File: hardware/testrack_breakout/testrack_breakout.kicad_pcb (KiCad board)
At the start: 4 copper layers, 40 x 78 mm, 15 parts, among them J1 USB_C_Receptacle_USB2.0_16P, J2 Conn_02x05_Odd_Even, J3 Conn_02x10_Odd_Even, J4 Conn_01x04, J5 Conn_02x09_Odd_Even

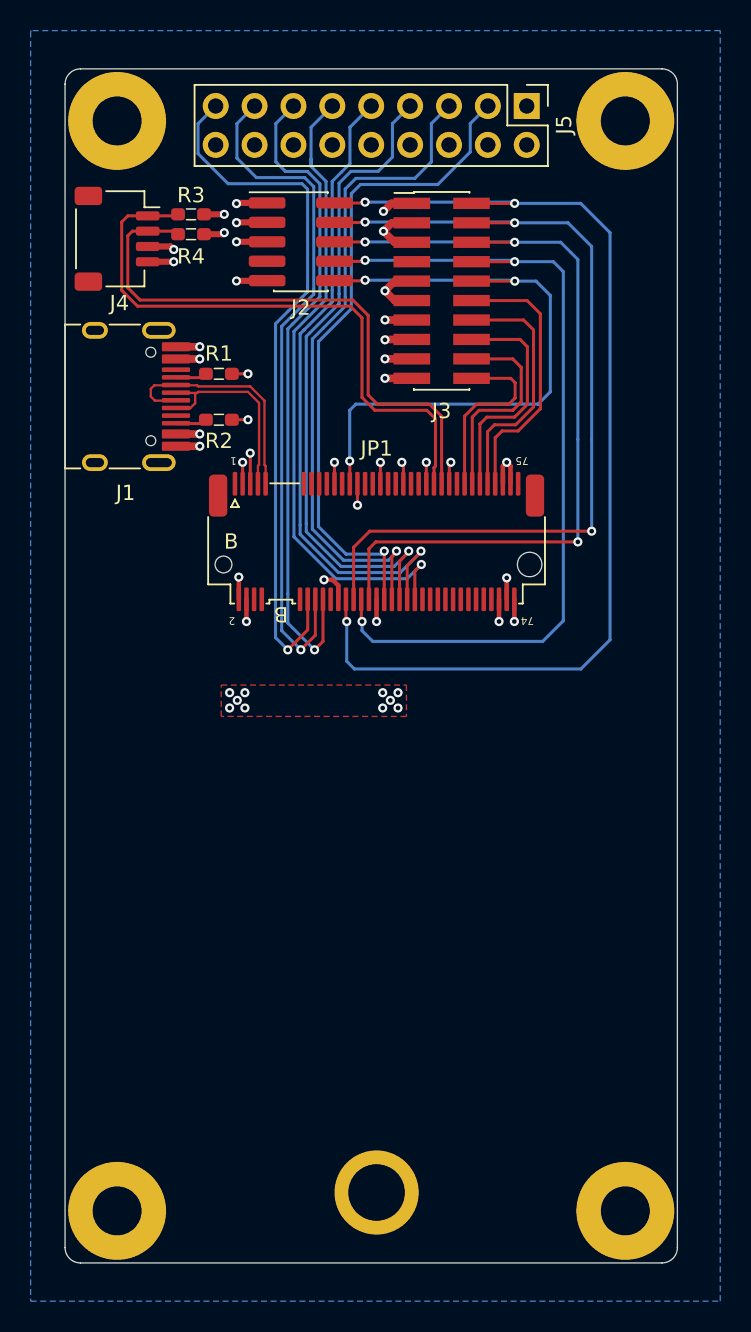
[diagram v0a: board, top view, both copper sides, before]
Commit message: Added board identification to the silkscreen
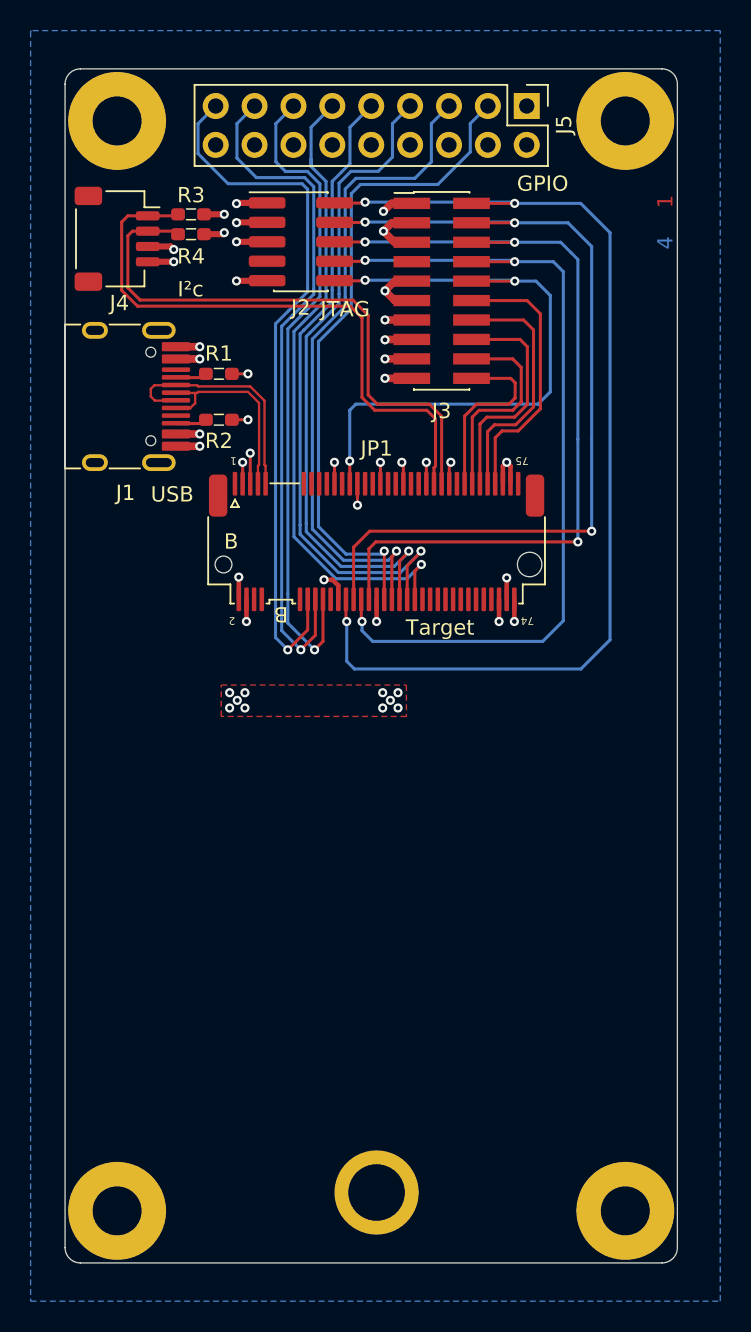
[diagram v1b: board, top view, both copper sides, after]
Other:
- board text added: "1"
- board text added: "1BitSquared"
- board text added: "2"
- board text added: "3"
- board text added: "4"
- board text added: "CERN OHL v2 Strict"
- board text added: "GPIO"
- board text added: "I²c"
- board text added: "JTAG"
- board text added: "License"
- board text added: "RWK"
- board text added: "Target"
- board text added: "USB"
- board text added: "testrack_breakout"
- board text added: "v0.1a"
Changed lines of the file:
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@@
 		(embedded_fonts no)
 	)
+	(gr_rect
+		(start 88.6 58.5)
+		(end 90.1 62.3)
+		(stroke
+			(width 0)
+			(type solid)
+		)
+		(fill yes)
+		(layer "F.Mask")
+	)
+	(gr_rect
+		(start 88.6 58.5)
+		(end 90.1 62.3)
+		(stroke
+			(width 0)
+			(type solid)
+		)
+		(fill yes)
+		(layer "B.Mask")
+	)
+	(gr_line
+		(start 70.2 98.5)
+		(end 70.2 110.6)
+		(stroke
+			(width 0.1)
+			(type default)
+		)
+		(layer "B.SilkS")
+	)
+	(gr_rect
+		(start 67.6 107)
+		(end 69.6 109.1)
+		(stroke
+			(width 0)
+			(type solid)
+		)
+		(fill yes)
+		(layer "B.SilkS")
+	)
 	(gr_arc
 		(start 90.2 127.5)
@@
 		(layer "Edge.Cuts")
 	)
+	(gr_text "1"
+		(at 90 59.6 90)
+		(layer "F.Cu")
+		(effects
+			(font
+				(size 1 1)
+				(thickness 0.15)
+			)
+			(justify left bottom)
+		)
+	)
+	(gr_text "4"
+		(at 90 62.3 90)
+		(layer "B.Cu")
+		(effects
+			(font
+				(size 1 1)
+				(thickness 0.15)
+			)
+			(justify left bottom)
+		)
+	)
+	(gr_text "2"
+		(at 90 60.5 90)
+		(layer "In1.Cu")
+		(effects
+			(font
+				(size 1 1)
+				(thickness 0.15)
+			)
+			(justify left bottom)
+		)
+	)
+	(gr_text "I²c"
+		(at 58.4 64.9 0)
+		(layer "F.SilkS")
+		(effects
+			(font
+				(size 1 1)
+				(thickness 0.1)
+			)
+		)
+	)
+	(gr_text "GPIO"
+		(at 81.4 58 0)
+		(layer "F.SilkS")
+		(effects
+			(font
+				(size 1 1)
+				(thickness 0.1)
+			)
+		)
+	)
+	(gr_text "JTAG"
+		(at 68.5 66.2 0)
+		(layer "F.SilkS")
+		(effects
+			(font
+				(size 1 1)
+				(thickness 0.1)
+			)
+		)
+	)
+	(gr_text "Target"
+		(at 74.7 87 0)
+		(layer "F.SilkS")
+		(effects
+			(font
+				(size 1 1)
+				(thickness 0.1)
+			)
+		)
+	)
+	(gr_text "USB"
+		(at 57.2 78.3 0)
+		(layer "F.SilkS")
+		(effects
+			(font
+				(size 1 1)
+				(thickness 0.1)
+			)
+		)
+	)
+	(gr_text "3"
+		(at 90 61.4 90)
+		(layer "In2.Cu")
+		(effects
+			(font
+				(size 1 1)
+				(thickness 0.15)
+			)
+			(justify left bottom)
+		)
+	)
+	(gr_text "1BitSquared"
+		(at 70 99.8 -0)
+		(layer "B.SilkS")
+		(effects
+			(font
+				(size 1 1)
+				(thickness 0.1)
+			)
+			(justify left mirror)
+		)
+	)
+	(gr_text "testrack_breakout"
+		(at 70.4 99.8 0)
+		(layer "B.SilkS")
+		(effects
+			(font
+				(size 1 1)
+				(thickness 0.1)
+			)
+			(justify right mirror)
+		)
+	)
+	(gr_text "v0.1a"
+		(at 70.4 101.4 -0)
+		(layer "B.SilkS")
+		(effects
+			(font
+				(size 1 1)
+				(thickness 0.1)
+			)
+			(justify right mirror)
+		)
+	)
+	(gr_text "RWK"
+		(at 70.4 108.7 0)
+		(layer "B.SilkS")
+		(effects
+			(font
+				(size 1 1)
+				(thickness 0.1)
+			)
+			(justify right bottom mirror)
+		)
+	)
+	(gr_text "CERN OHL\nv2 Strict"
+		(at 69.7 104.7 -0)
+		(layer "B.SilkS")
+		(effects
+			(font
+				(size 1 1)
+				(thickness 0.1)
+			)
+			(justify left mirror)
+		)
+	)
+	(gr_text "License"
+		(at 70.7 103.9 -0)
+		(layer "B.SilkS")
+		(effects
+			(font
+				(size 1 1)
+				(thickness 0.1)
+			)
+			(justify right mirror)
+		)
+	)
 	(segment
 		(start 63.4 64.345)
@@
 			)
 		)
+	)
+	(zone
+		(net 0)
+		(net_name "")
+		(layers "F.Cu" "F.Mask" "B.Cu" "B.Mask" "In1.Cu" "In2.Cu")
+		(hatch edge 0.5)
+		(connect_pads
+			(clearance 0)
+		)
+		(min_thickness 0.25)
+		(filled_areas_thickness no)
+		(keepout
+			(tracks not_allowed)
+			(vias not_allowed)
+			(pads not_allowed)
+			(copperpour not_allowed)
+			(footprints not_allowed)
+		)
+		(placement
+			(enabled no)
+			(sheetname "/")
+		)
+		(fill
+			(thermal_gap 0.5)
+			(thermal_bridge_width 0.5)
+		)
+		(polygon
+			(pts
+				(xy 88.5 58.4) (xy 90.3 58.4) (xy 90.3 62.5) (xy 88.5 62.5)
+			)
+		)
